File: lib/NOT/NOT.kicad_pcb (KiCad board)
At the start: 2 copper layers, 2 parts, among them P1 Q_PJFET_GSD

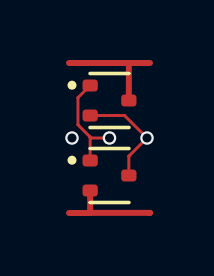
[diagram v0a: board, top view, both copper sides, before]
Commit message: The layout of the NOT gate was also botched (PMOS pinout wrong)
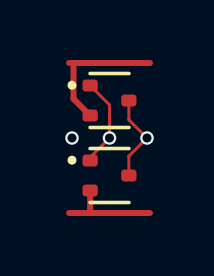
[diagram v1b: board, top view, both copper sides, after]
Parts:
- N1: value Q_NJFET_GSD -> (none)
- P1: value Q_PJFET_GSD -> (none)
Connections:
- P1 pad 2: Y -> VDD
- P1 pad 3: VDD -> Y
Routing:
- net VDD: track 3.95 -> 4.68 mm
- net Y: track 3.71 -> 3.00 mm
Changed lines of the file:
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@@
 			)
 		)
-		(property "Value" "Q_PJFET_GSD"
+		(property "Value" ""
 			(at 0 1.75 0)
 			(layer "F.Fab")
@@
 			)
 		)
-		(sheetname "/")
-		(sheetfile "NOT.kicad_sch")
 		(attr smd)
 		(fp_line
@@
 			(net 3 "A")
 			(pinfunction "G")
-			(pintype "input")
+			(pintype "inout")
 		)
 		(pad "2" smd roundrect
@@
 			(layers "F.Cu" "F.Mask" "F.Paste")
 			(roundrect_rratio 0.25)
-			(net 1 "Y")
+			(net 4 "VDD")
 			(pinfunction "S")
-			(pintype "passive")
+			(pintype "inout")
 		)
 		(pad "3" smd roundrect
@@
 			(layers "F.Cu" "F.Mask" "F.Paste")
 			(roundrect_rratio 0.25)
-			(net 4 "VDD")
+			(net 1 "Y")
 			(pinfunction "D")
-			(pintype "passive")
+			(pintype "inout")
 		)
 		(embedded_fonts no)
@@
 			)
 		)
-		(property "Value" "Q_NJFET_GSD"
+		(property "Value" ""
 			(at 0 1.75 0)
 			(layer "F.Fab")
@@
 			)
 		)
-		(sheetname "/")
-		(sheetfile "NOT.kicad_sch")
 		(attr smd)
 		(fp_line
@@
 			(net 3 "A")
 			(pinfunction "G")
-			(pintype "input")
+			(pintype "inout")
 		)
 		(pad "2" smd roundrect
@@
 			(net 2 "GND")
 			(pinfunction "S")
-			(pintype "passive")
+			(pintype "inout")
 		)
 		(pad "3" smd roundrect
@@
 			(net 1 "Y")
 			(pinfunction "D")
-			(pintype "passive")
+			(pintype "inout")
 		)
 		(embedded_fonts no)
@@
 	)
 	(segment
+		(start 1.895 1.895)
+		(end 2.5 2.5)
+		(width 0.1)
+		(layer "F.Cu")
+		(net 1)
+	)
+	(segment
+		(start 1.895 1.25)
+		(end 1.895 1.895)
+		(width 0.1)
+		(layer "F.Cu")
+		(net 1)
+	)
+	(segment
+		(start 2.5 2.5)
+		(end 1.895 3.105)
+		(width 0.1)
+		(layer "F.Cu")
+		(net 1)
+	)
+	(segment
 		(start 1.895 3.105)
 		(end 1.895 3.75)
-		(width 0.1)
-		(layer "F.Cu")
-		(net 1)
-	)
-	(segment
-		(start 1.75 1.75)
-		(end 2.5 2.5)
-		(width 0.1)
-		(layer "F.Cu")
-		(net 1)
-	)
-	(segment
-		(start 0.605 1.75)
-		(end 1.75 1.75)
-		(width 0.1)
-		(layer "F.Cu")
-		(net 1)
-	)
-	(segment
-		(start 2.5 2.5)
-		(end 1.895 3.105)
 		(width 0.1)
 		(layer "F.Cu")
@@
 	)
 	(segment
-		(start 0.605 4.995)
-		(end 2.595 4.995)
+		(start 0.605 5)
+		(end 2.6 5)
+		(width 0.2)
+		(layer "F.Cu")
+		(net 2)
+	)
+	(segment
+		(start 0.6 5)
+		(end -0.1 5)
 		(width 0.2)
 		(layer "F.Cu")
@@
 	)
 	(segment
-		(start 2.595 4.995)
-		(end 2.6 5)
-		(width 0.2)
-		(layer "F.Cu")
-		(net 2)
-	)
-	(segment
 		(start 0.605 4.25)
 		(end 0.605 4.995)
@@
 	)
 	(segment
-		(start 0.6 5)
-		(end -0.1 5)
-		(width 0.2)
-		(layer "F.Cu")
-		(net 2)
-	)
-	(segment
-		(start 0.605 2.467189)
+		(start 1.25 2.5)
+		(end 0.605 3.145)
+		(width 0.1)
+		(layer "F.Cu")
+		(net 3)
+	)
+	(segment
+		(start 0.605 0.75)
+		(end 1.25 1.395)
+		(width 0.1)
+		(layer "F.Cu")
+		(net 3)
+	)
+	(segment
+		(start 1.25 1.395)
+		(end 1.25 2.5)
+		(width 0.1)
+		(layer "F.Cu")
+		(net 3)
+	)
+	(segment
+		(start 0.605 3.145)
 		(end 0.605 3.25)
-		(width 0.1)
-		(layer "F.Cu")
-		(net 3)
-	)
-	(segment
-		(start 0.199 2.061189)
-		(end 0.605 2.467189)
-		(width 0.1)
-		(layer "F.Cu")
-		(net 3)
-	)
-	(segment
-		(start 0.637811 2.5)
-		(end 0.605 2.467189)
-		(width 0.1)
-		(layer "F.Cu")
-		(net 3)
-	)
-	(segment
-		(start 0.199 1.156)
-		(end 0.199 2.061189)
-		(width 0.1)
-		(layer "F.Cu")
-		(net 3)
-	)
-	(segment
-		(start 1.25 2.5)
-		(end 0.637811 2.5)
-		(width 0.1)
-		(layer "F.Cu")
-		(net 3)
-	)
-	(segment
-		(start 0.605 0.75)
-		(end 0.199 1.156)
 		(width 0.1)
 		(layer "F.Cu")
@@
 	)
 	(segment
+		(start 0.605 1.75)
+		(end 0.05 1.195)
+		(width 0.2)
+		(layer "F.Cu")
+		(net 4)
+	)
+	(segment
+		(start 0.05 1.195)
+		(end 0.05 0)
+		(width 0.2)
+		(layer "F.Cu")
+		(net 4)
+	)
+	(segment
 		(start 1.9 0)
+		(end 0.05 0)
+		(width 0.2)
+		(layer "F.Cu")
+		(net 4)
+	)
+	(segment
+		(start 0.05 0)
 		(end -0.1 0)
 		(width 0.2)
 		(layer "F.Cu")
-		(net 4)
-	)
-	(segment
-		(start 1.895 1.25)
-		(end 1.895 0.005)
-		(width 0.2)
-		(layer "F.Cu")

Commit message: High-density layout with pitch of 1.1mm, which gains 23% !!
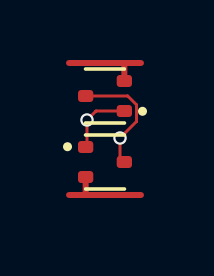
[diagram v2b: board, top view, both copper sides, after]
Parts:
- moved N1 0.47 mm to (1.10, 3.30)
- moved P1 0.21 mm to (1.10, 1.10), turned to 180 degrees
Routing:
- net VDD: track 4.68 -> 3.00 mm
- net Y: track 3.00 -> 4.01 mm
- net A: track 3.03 -> 2.29 mm
- net (no net): vias 1 -> 0

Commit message: All cells now use 1mm*4mm grid rather than 1.1mm*4.4mm
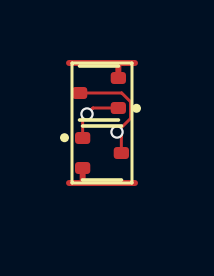
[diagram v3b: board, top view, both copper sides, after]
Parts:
- moved N1 0.32 mm to (1.00, 3.00)
- moved P1 0.22 mm to (0.90, 1.00)
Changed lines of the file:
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@@
 	(footprint "Package_TO_SOT_SMD:SOT-523"
 		(layer "F.Cu")
-		(at 1.1 1.1 180)
+		(at 0.9 1 180)
 		(descr "SOT523, https://www.diodes.com/assets/Package-Files/SOT523.pdf")
 		(tags "SOT-523")
@@
 	(footprint "Package_TO_SOT_SMD:SOT-523"
 		(layer "F.Cu")
-		(at 1.1 3.3)
+		(at 1 3)
 		(descr "SOT523, https://www.diodes.com/assets/Package-Files/SOT523.pdf")
 		(tags "SOT-523")
@@
 		)
 	)
-	(segment
-		(start 1.857738 1.1)
-		(end 2.151 1.393262)
+	(gr_rect
+		(start 0 0)
+		(end 2 4)
+		(stroke
+			(width 0.1)
+			(type default)
+		)
+		(fill no)
+		(layer "F.SilkS")
+	)
+	(segment
+		(start 1.951 1.849)
+		(end 1.5 2.3)
 		(width 0.1)
 		(layer "F.Cu")
@@
 	)
 	(segment
-		(start 1.6 3.155)
-		(end 1.745 3.3)
+		(start 1.645 3)
+		(end 1.645 2.445)
 		(width 0.1)
 		(layer "F.Cu")
@@
 	)
 	(segment
-		(start 1.6 2.5)
-		(end 1.6 3.155)
+		(start 1.657738 1)
+		(end 1.951 1.293262)
 		(width 0.1)
 		(layer "F.Cu")
@@
 	)
 	(segment
-		(start 2.151 1.393262)
-		(end 2.151 1.949)
+		(start 0.355 1)
+		(end 1.657738 1)
 		(width 0.1)
 		(layer "F.Cu")
@@
 	)
 	(segment
-		(start 0.455 1.1)
-		(end 1.857738 1.1)
+		(start 1.951 1.293262)
+		(end 1.951 1.849)
 		(width 0.1)
 		(layer "F.Cu")
@@
 	)
 	(segment
-		(start 2.151 1.949)
-		(end 1.6 2.5)
+		(start 1.645 2.445)
+		(end 1.5 2.3)
 		(width 0.1)
 		(layer "F.Cu")
@@
 	)
 	(via
-		(at 1.6 2.5)
+		(at 1.5 2.3)
 		(size 0.45)
 		(drill 0.3)
@@
 	)
 	(segment
-		(start 0.605 4.4)
-		(end 2.3 4.4)
+		(start 0.605 4)
+		(end 2.1 4)
 		(width 0.2)
 		(layer "F.Cu")
@@
 	)
 	(segment
-		(start 0.44 4.4)
-		(end -0.1 4.4)
+		(start 0.44 4)
+		(end 0.34 4)
 		(width 0.2)
 		(layer "F.Cu")
@@
 	)
 	(segment
-		(start 0.6 4.4)
-		(end 0.44 4.4)
+		(start 0.355 3.985)
+		(end 0.34 4)
 		(width 0.2)
 		(layer "F.Cu")
@@
 	)
 	(segment
-		(start 0.455 4.385)
-		(end 0.44 4.4)
+		(start 0.34 4)
+		(end -0.1 4)
 		(width 0.2)
 		(layer "F.Cu")
@@
 	)
 	(segment
-		(start 0.455 3.8)
-		(end 0.455 4.385)
+		(start 0.6 4)
+		(end 0.44 4)
 		(width 0.2)
 		(layer "F.Cu")
@@
 	)
 	(segment
-		(start 0.8 1.6)
-		(end 0.5 1.9)
+		(start 0.355 3.5)
+		(end 0.355 3.985)
+		(width 0.2)
+		(layer "F.Cu")
+		(net 2)
+	)
+	(segment
+		(start 0.7 1.5)
+		(end 0.5 1.7)
 		(width 0.1)
 		(layer "F.Cu")
@@
 	)
 	(segment
-		(start 1.745 1.6)
-		(end 0.8 1.6)
+		(start 0.355 1.845)
+		(end 0.5 1.7)
 		(width 0.1)
 		(layer "F.Cu")
@@
 	)
 	(segment
-		(start 0.5 1.9)
-		(end 0.5 2.755)
+		(start 0.355 2.5)
+		(end 0.355 1.845)
 		(width 0.1)
 		(layer "F.Cu")
@@
 	)
 	(segment
-		(start 0.5 2.755)
-		(end 0.455 2.8)
+		(start 1.545 1.5)
+		(end 0.7 1.5)
 		(width 0.1)
 		(layer "F.Cu")
@@
 	)
 	(via
-		(at 0.5 1.9)
+		(at 0.5 1.7)
 		(size 0.45)
 		(drill 0.3)
@@
 	)
 	(segment
+		(start 1.545 0.5)
+		(end 1.545 0.045)
+		(width 0.2)
+		(layer "F.Cu")
+		(net 4)
+	)
+	(segment
+		(start 1.5 0)
+		(end 1.64 0)
+		(width 0.2)
+		(layer "F.Cu")
+		(net 4)
+	)
+	(segment
+		(start 1.645 0.005)
+		(end 1.64 0)
+		(width 0.2)
+		(layer "F.Cu")
+		(net 4)
+	)
+	(segment
 		(start 1.75 0)
-		(end 2.3 0)
+		(end 2.1 0)
 		(width 0.2)
 		(layer "F.Cu")
@@
 	)
 	(segment
-		(start 1.745 0.6)
-		(end 1.745 0.005)
-		(width 0.2)
-		(layer "F.Cu")
-		(net 4)
-	)
-	(segment
 		(start -0.1 0)
-		(end 1.75 0)
+		(end 1.5 0)
 		(width 0.2)
 		(layer "F.Cu")
@@
 		(end 1.75 0)
 		(width 0.2)
+		(layer "F.Cu")
+		(net 4)
+	)
+	(segment
+		(start 1.545 0.045)
+		(end 1.5 0)
+		(width 0.2)
+		(layer "F.Cu")
+		(net 4)
+	)
+	(segment
+		(start 1.64 0)
+		(end 1.75 0)
+		(width 0.2)

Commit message: Make the pads of my SOT523 footprint very slightly smaller, which is enough to route all the cells and leave the mosfets exactly on the grid
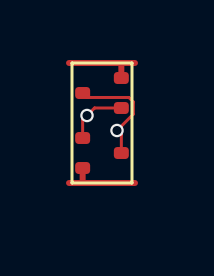
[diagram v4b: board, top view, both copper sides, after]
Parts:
- N1, P1: footprint Package_TO_SOT_SMD:SOT-523 -> RV523:SOT523
- moved P1 0.10 mm to (1.00, 1.00)

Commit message: Propagate MOSFET values to the cells' PCBs
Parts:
- N1: value (none) -> NMOS
- P1: value (none) -> PMOS
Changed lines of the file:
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@@
 			)
 		)
-		(property "Value" ""
+		(property "Value" "PMOS"
 			(at 0 0 180)
 			(layer "F.Fab")
@@
 			)
 		)
-		(property "Value" ""
+		(property "Value" "NMOS"
 			(at 0 0 0)
 			(layer "F.Fab")
